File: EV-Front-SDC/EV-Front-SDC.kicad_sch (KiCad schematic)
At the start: 27 parts, among them J1 JST-XA, J2 JST-XA, J3 JST-XA, J4 JST-XA, J5 JST-XA, J6 IMU, J7 GPS, J8 Conn_01x14, Q1 BSS205N, Q2 BSS205N, Q3 BSS205N, U2 MCP23S08-E_SS

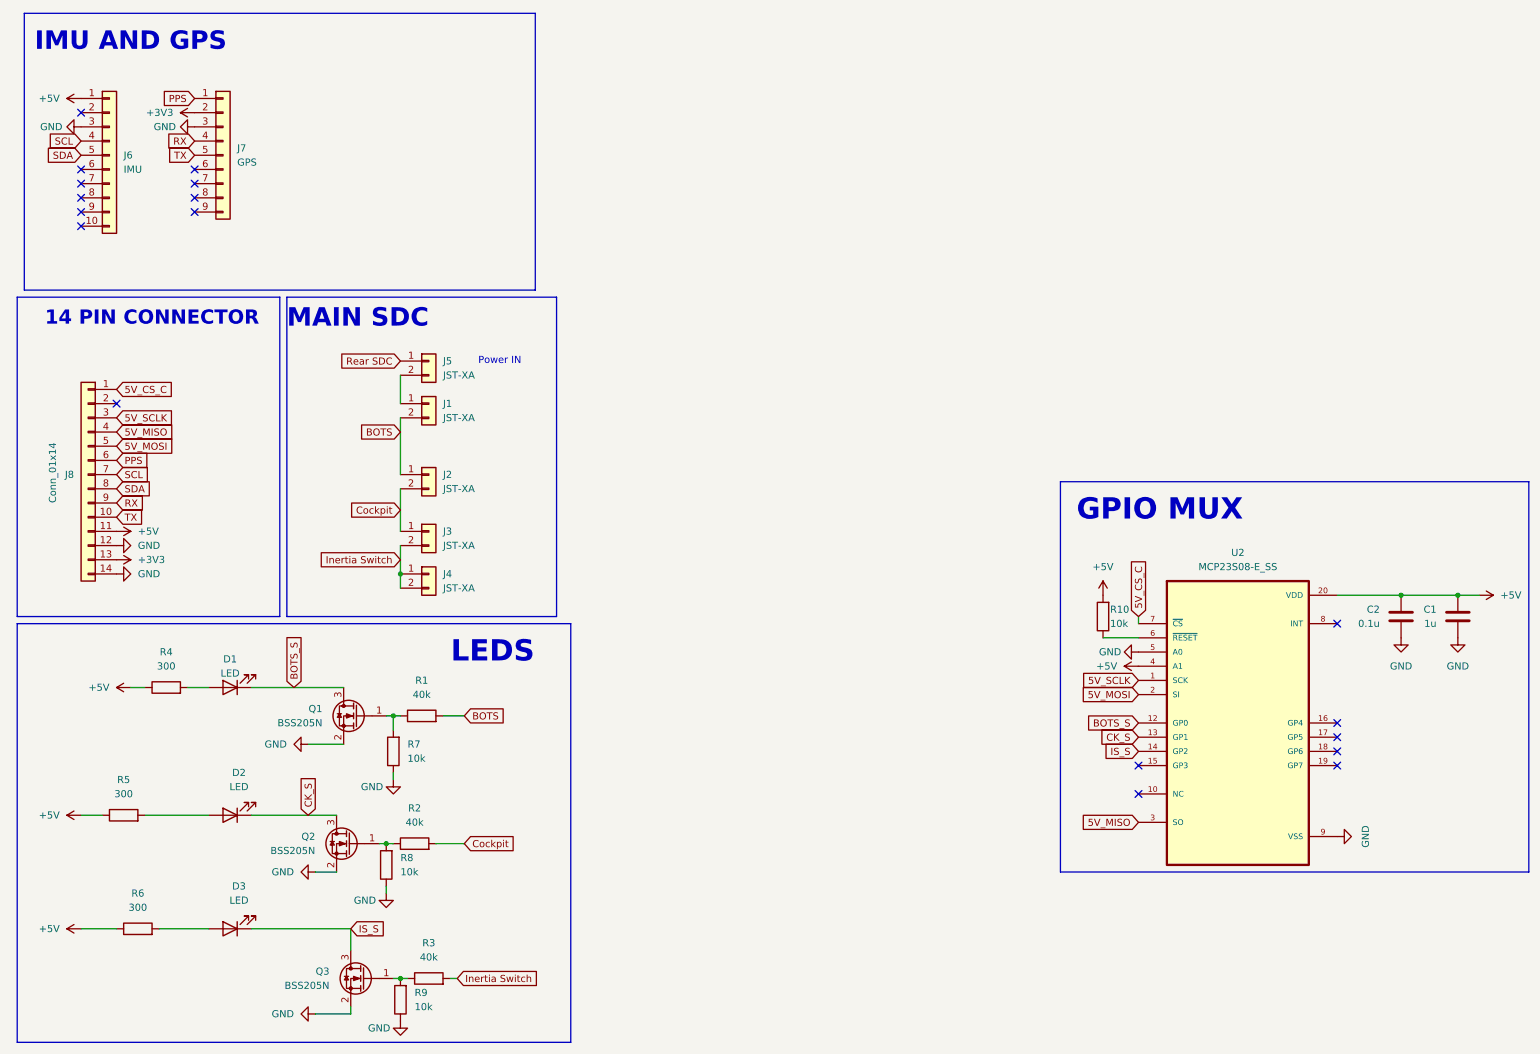
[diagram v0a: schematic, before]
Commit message: - SDC loop now on one connector - Added new IMU
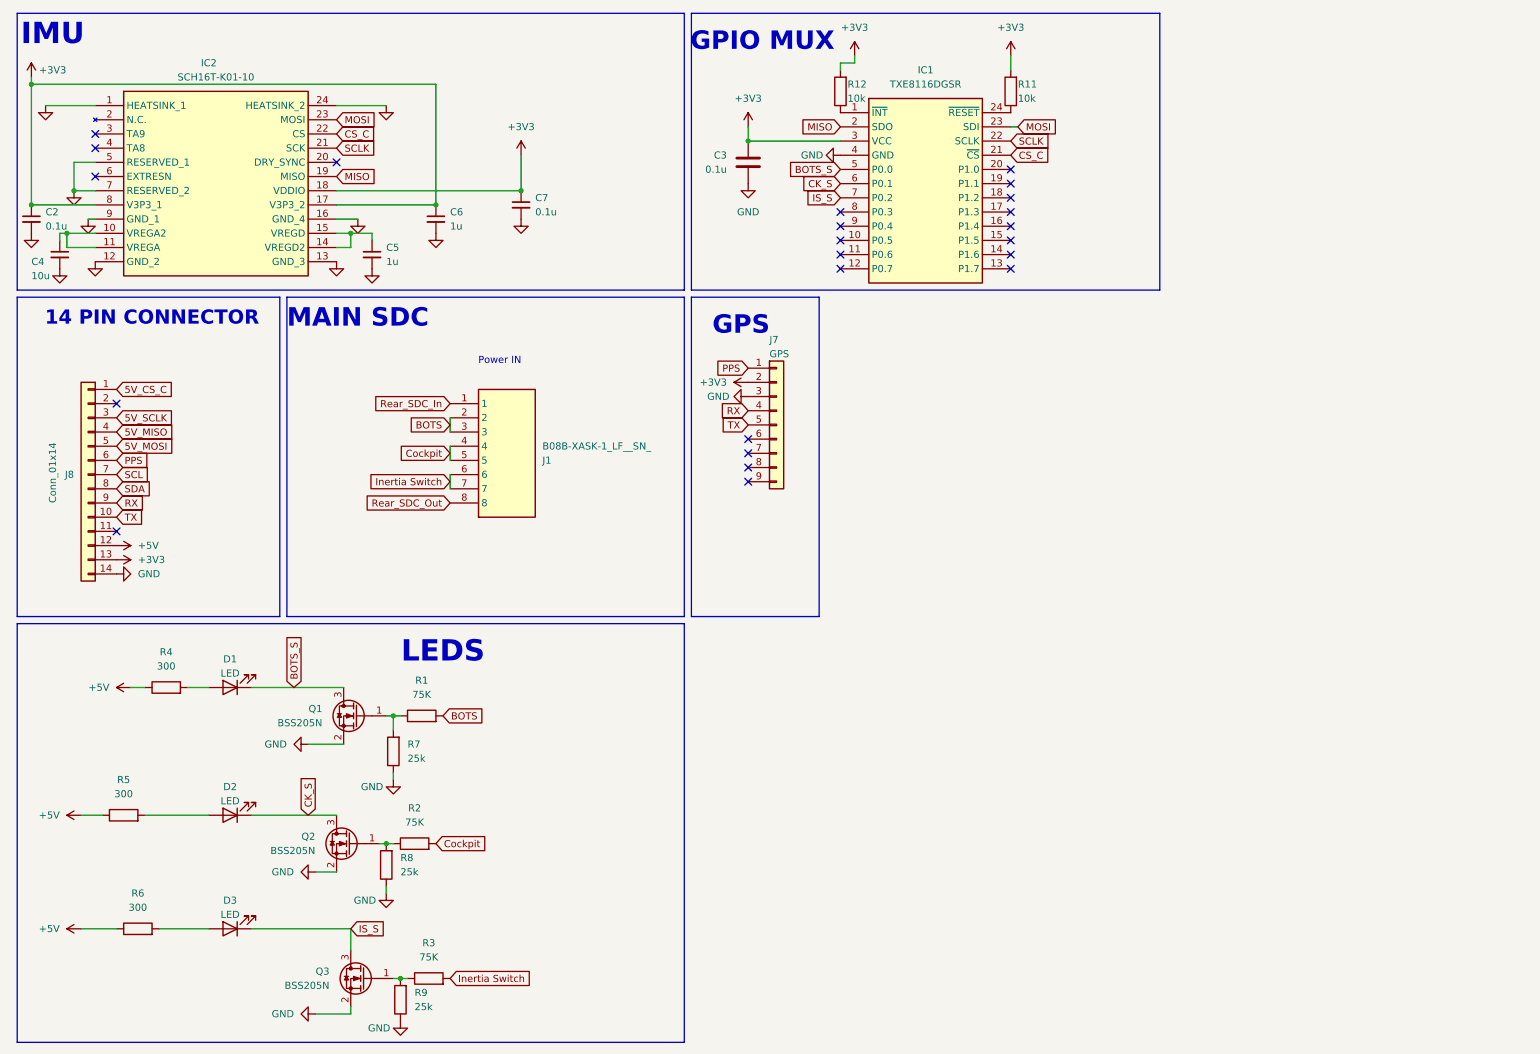
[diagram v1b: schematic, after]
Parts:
- removed C1: 1u, symbol Device:C
- removed C2: 0.1u, symbol Device:C
- removed J1, J2, J3, J4, J5: JST-XA, Custom_MSM:Connector_JST-XA_2POS, symbol Custom_MSM1:Connector_JST-XA_2POS
- removed J6: IMU, CustomFootprints10:IMU, symbol Connector_Generic:Conn_01x10
- removed R10: 10k, symbol Device:R
- removed U2: MCP23S08-E_SS, symbol MCP23S08-E_SS:MCP23S08-E_SS
- added C2, C7: 0.1u, Capacitor_SMD:C_0603_1608Metric, symbol Device:C_Small
- added C3: 0.1u, Capacitor_SMD:C_0603_1608Metric, symbol Device:C
- added C4: 10u, Capacitor_SMD:C_0603_1608Metric, symbol Device:C_Small
- added C5, C6: 1u, Capacitor_SMD:C_0603_1608Metric, symbol Device:C_Small
- added IC1: TXE8116DGSR, SOP50P490X110-24N, symbol Custom_MSM1:TXE8116DGSR
- added IC2: SCH16T-K01-10, Custom_MSM:SCH16TK0110, symbol SCH16T-K01-10:SCH16T-K01-10
- added J1: B08B-XASK-1_LF__SN_, B08BXASK1LFSN, symbol B08B-XASK-1_LF__SN_:B08B-XASK-1_LF__SN_
- added R11, R12: 10k, Resistor_SMD:R_0603_1608Metric, symbol Device:R
- D1, D2, D3: footprint (none) -> LED_SMD:LED_0603_1608Metric; MFN (none) -> LR Q976.01; S1PL (none) -> https://www.mouser.co.uk/en/ProductDetail/ams-OSRAM/LR-Q976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; S1PN (none) -> 720-LRQ976.01; S2PL (none) -> http://digikey.co.uk/en/products/detail/ams-osram-ag/LR-Q97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; S2PN (none) -> 475-LRQ976.01-P2R2-1CT-ND
- J8: MFN (none) -> B14B-XASK-1 (LF)(SN); S1PL (none) -> https://uk.rs-online.com/web/p/pcb-headers/6027837; S1PN (none) -> 602-7837
- R1, R2, R3: value 40k -> 75K; footprint (none) -> Resistor_SMD:R_0603_1608Metric; MFN (none) -> TNPW060375K0BHEA; S1PL (none) -> https://www.mouser.co.uk/en/ProductDetail/Vishay/TNPW060375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; S1PN (none) -> 71-TNPW060375K0BHEA; S2PL (none) -> https://www.digikey.co.uk/en/products/detail/vishay-dale/tn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; S2PN (none) -> 541-TNPW060375K0BHEACT-ND
- R4, R5, R6: footprint (none) -> Resistor_SMD:R_0603_1608Metric; MFN (none) -> CRCW0603300RJNEAHP; S1PL (none) -> https://www.mouser.co.uk/en/ProductDetail/Vishay/CRCW060330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; S1PN (none) -> 71-CRCW0603300RJNEAH; S2PL (none) -> https://www.digikey.co.uk/en/products/detail/vishay-dale/CR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; S2PN (none) -> 541-300SATR-ND
- R7, R8, R9: value 10k -> 25k; footprint (none) -> Resistor_SMD:R_0603_1608Metric; MFN (none) -> PTN0603H2502BST1; S1PL (none) -> https://www.mouser.co.uk/en/ProductDetail/Vishay-Thin-Film/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; S1PN (none) -> Images are for reference only See Product Specifications Mo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
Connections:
- net +3V3: now also C2.1, C3.1, C6.1, C7.1, IC1.3 (VCC), IC2.17 (V3P3_2), IC2.18 (VDDIO), IC2.8 (V3P3_1), R11.2, R12.2
- net +5V: now also J8.12 (Pin_12); no longer J8.11 (Pin_11)
- net BOTS: now also J1.2, J1.3
- net BOTS_S: now also IC1.5 (P0.0)
- net CK_S: now also IC1.6 (P0.1)
- net Cockpit: now also J1.4, J1.5
- net GND: now also C2.2, C3.2, C4.2, C5.2, C6.2, C7.2, IC1.4 (GND), IC2.1 (HEATSINK_1), IC2.12 (GND_2), IC2.13 (GND_3), IC2.16 (GND_4), IC2.24 (HEATSINK_2), IC2.5 (RESERVED_1), IC2.7 (RESERVED_2), IC2.9 (GND_1); no longer J8.12 (Pin_12)
- net IS_S: now also IC1.7 (P0.2)
- net Inertia Switch: now also J1.6, J1.7
- new net: IC1.1 (~{INT}), R12.1
- new net: IC1.24 (~{RESET}), R11.1
- new net: C4.1, IC2.10 (VREGA2), IC2.11 (VREGA)
- new net: C5.1, IC2.14 (VREGD2), IC2.15 (VREGD)
- new net CS_C: IC1.21 (~{CS}), IC2.22 (CS)
- new net MISO: IC1.2 (SDO), IC2.19 (MISO)
- new net MOSI: IC1.23 (SDI), IC2.23 (MOSI)
- new net Rear_SDC_In: J1.1
- new net Rear_SDC_Out: J1.8
- new net SCLK: IC1.22 (SCLK), IC2.21 (SCK)
- no-connect marks 18 -> 23
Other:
- note added: "GPS"
- note added: "IMU"
- note removed: "IMU AND GPS"

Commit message: Add files via upload
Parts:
- added C11, C12: 0.1u, Capacitor_SMD:C_0603_1608Metric, symbol Device:C
- added C13: 1u, Capacitor_SMD:C_0603_1608Metric, symbol Device:C
- added U3: MAX3390EEUD_T, customFootprints:SOP65P640X110-14N, symbol MAX3390EEUD_T:MAX3390EEUD_T
- U1: renamed from IC1; Mouser Part Number (none) -> 595-TXE8116DGSR; Mouser Price/Stock (none) -> https://www.mouser.co.uk/en/ProductDetail/Texas-Instruments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
- renumbered J7 to J2, J8 to J3, IC2 to U2
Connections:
- net +3V3: now also C11.1, U3.1 (VL), U3.8 (~{THREE}-STATE); no longer R11.2, R12.2
- net +5V: now also R11.2, R12.2, C12.1, C13.1, U3.14 (VCC)
- net 5V_MISO: now also U3.13 (I_VCC1)
- net 5V_MOSI: now also U3.12 (O_VCC2)
- net 5V_SCLK: now also U3.11 (O_VCC3)
- net CS_C: no longer U2.22 (CS)
- net GND: now also C11.2, U3.7 (GND)
- net MISO: now also U3.2 (O_VL1)
- net MOSI: now also U3.3 (I_VL2)
- net SCLK: now also U3.4 (I_VL3)
- net 5V_CS_D: now reaches J3.2 (Pin_2)
- net 5V_CS_D: now also U3.10 (O_VCC4)
- net SCL: no longer names the net of J3.7 (Pin_7)
- net SDA: no longer names the net of J3.8 (Pin_8)
- new net: C12.2, C13.2
- new net CS_D: U2.22 (CS), U3.5 (I_VL4)
- no-connect marks 23 -> 22
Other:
- note added: "Level-Shifter"

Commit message: Made SDC Routing changes
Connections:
- net Inertia Switch: no longer J1.6, J1.7
- net Rear_SDC_Out: no longer names the net of J1.8
- new net Inertia Switch (Out): J1.6
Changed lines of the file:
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@@
-	(wire
-		(pts
-			(xy 90.17 95.25) (xy 90.17 97.79)
-		)
-		(stroke
-			(width 0)
-			(type default)
-		)
-	)
 	(wire
 		(pts
@@
 		)
 	)
-	(global_label "Rear_SDC_Out"
-		(shape input)
-		(at 90.17 100.33 180)
-		(effects
-			(font
-				(size 1.27 1.27)
-			)
-			(justify right)
-		)
-		(property "Intersheetrefs" "${INTERSHEET_REFS}"
-			(at 81.8025 109.22 0)
-			(hide yes)
-			(show_name no)
-			(do_not_autoplace no)
-			(effects
-				(font
-					(size 1.27 1.27)
-				)
-				(justify right)
-			)
-		)
-	)
 	(global_label "5V_SCLK"
 		(shape input)
@@
 		)
 	)
-	(global_label "Inertia Switch"
-		(shape input)
-		(at 90.17 96.52 180)
-		(fields_autoplaced yes)
-		(effects
-			(font
-				(size 1.27 1.27)
-			)
-			(justify right)
-		)
-		(property "Intersheetrefs" "${INTERSHEET_REFS}"
-			(at 82.4072 96.52 0)
-			(hide yes)
-			(show_name no)
-			(do_not_autoplace no)
-			(effects
-				(font
-					(size 1.27 1.27)
-				)
-				(justify right)
-			)
-		)
-	)
 	(global_label "5V_CS_D"
 		(shape input)
@@
 			)
 		)
+	)
+	(global_label "Inertia Switch (Out)"
+		(shape input)
+		(at 90.17 95.25 180)
+		(effects
+			(font
+				(size 1.27 1.27)
+			)
+			(justify right)
+		)
+		(property "Intersheetrefs" "${INTERSHEET_REFS}"
+			(at 81.8025 104.14 0)
+			(hide yes)
+			(show_name no)
+			(do_not_autoplace no)
+			(effects
+				(font
+					(size 1.27 1.27)
+				)
+				(justify right)
+			)
+		)

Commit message: Routed the PCB
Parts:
- removed J1: B08B-XASK-1_LF__SN_, B08BXASK1LFSN, symbol B08B-XASK-1_LF__SN_:B08B-XASK-1_LF__SN_
- added J1: B06B-PASK_LF__SN_, Custom_MSM:S06BXASK1LFSN, symbol B06B-PASK_LF__SN_:B06B-PASK_LF__SN_
- C11, C12, C13, C2, C3, C4, C5, C6, C7: footprint Capacitor_SMD:C_0603_1608Metric -> Capacitor_SMD:C_0805_2012Metric
- D1, D2, D3: footprint LED_SMD:LED_0603_1608Metric -> LED_SMD:LED_0805_2012Metric
- R1, R11, R12, R2, R3, R4, R5, R6, R7, R8, R9: footprint Resistor_SMD:R_0603_1608Metric -> Resistor_SMD:R_0805_2012Metric
- U1: footprint SOP50P490X110-24N -> Package_DFN_QFN:QFN-24-1EP_4x4mm_P0.5mm_EP2.7x2.7mm
- U3: footprint customFootprints:SOP65P640X110-14N -> Custom_MSM:SOP65P640X110-14N
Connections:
- net CS_C is gone; now on net 5V_CS_C: U1.21 (~{CS})
- net +3V3: no longer C3.1, U1.3 (VCC)
- net +5V: now also C3.1, U1.3 (VCC)
- net 5V_MISO: now also U1.2 (SDO)
- net 5V_MOSI: now also U1.23 (SDI)
- net 5V_SCLK: now also U1.22 (SCLK)
- net BOTS: now also J1.2, J1.3
- net Cockpit: now also J1.4, J1.5
- net Inertia Switch: now also J1.6
- net MISO: no longer U1.2 (SDO)
- net MOSI: no longer U1.23 (SDI)
- net SCLK: no longer U1.22 (SCLK)
- new net Rear_SDC_In(Right): J1.1
- no-connect marks 22 -> 24

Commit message: Fixed GPIO footprint + added signature
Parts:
- removed U1: TXE8116DGSR, Package_DFN_QFN:QFN-24-1EP_4x4mm_P0.5mm_EP2.7x2.7mm, symbol Custom_MSM1:TXE8116DGSR
- added U1: (no value), Package_DFN_QFN:QFN-24-1EP_4x4mm_P0.5mm_EP2.7x2.7mm, symbol Custom_MSM1:TXE8116RGER
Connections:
- net +5V: now also U1.18 (VCC)
- net 5V_CS_C: now also U1.12 (CS)
- net 5V_MISO: now also U1.17 (SDO)
- net 5V_MOSI: now also U1.14 (SDI)
- net 5V_SCLK: now also U1.13 (SCLK)
- net BOTS_S: now also U1.20 (P0.0)
- net CK_S: now also U1.21 (P0.1)
- net GND: now also C12.2, C13.2, U1.19 (GND)
- net IS_S: now also U1.22 (P0.2)
- net at R12.1: now also U1.16 (INT)
- net at R11.1: now also U1.15 (RESET)

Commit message: Re-routed and bomed
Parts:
- removed C11, C12, C3: 0.1u, Capacitor_SMD:C_0805_2012Metric, symbol Device:C
- removed C13: 1u, Capacitor_SMD:C_0805_2012Metric, symbol Device:C
- removed C2: 0.1u, Capacitor_SMD:C_0805_2012Metric, symbol Device:C_Small
- removed J1: B06B-PASK_LF__SN_, Custom_MSM:S06BXASK1LFSN, symbol B06B-PASK_LF__SN_:B06B-PASK_LF__SN_
- removed U1: (no value), Package_DFN_QFN:QFN-24-1EP_4x4mm_P0.5mm_EP2.7x2.7mm, symbol Custom_MSM1:TXE8116RGER
- added C1, C7, C8: 0.1u, Capacitor_SMD:C_0805_2012Metric, symbol Device:C_Small
- added C4, C9: 1u, Capacitor_SMD:C_0805_2012Metric, symbol Device:C_Small
- added J2: Conn_01x06, Connector_JST:JST_XA_S06B-XASK-1_1x06_P2.50mm_Horizontal, symbol Connector_Generic:Conn_01x06
- added U2: (no value), Package_DFN_QFN:QFN-24-1EP_4x4mm_P0.5mm_EP2.7x2.7mm, symbol Custom_MSM1:TXE8116RGER
- C2: renamed from C4; MFP (none) -> VJ0805Y106KXQTW1BC; S1PL (none) -> https://www.mouser.co.uk/en/ProductDetail/Vishay-Vitramon/V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; S1PN (none) -> 77-VJ0805Y106KXQTWBC; S1PRICE (none) -> 0.361; S2PL (none) -> https://www.digikey.co.uk/en/products/detail/vishay-vitramo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; S2PN (none) -> 720-VJ0805Y106KXQTW1BCTR-ND; S2PRICE (none) -> 0.38
- C3: renamed from C5; MFP (none) -> VJ0805Y105KXQTW1BC; S1PL (none) -> https://www.mouser.co.uk/en/ProductDetail/Vishay-Vitramon/V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; S1PN (none) -> 77-VJ0805Y105KXQTBC; S1PRICE (none) -> 0.196; S2PL (none) -> https://www.digikey.co.uk/en/products/detail/vishay-vitramo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; S2PN (none) -> 720-1757-1-ND; S2PRICE (none) -> 0.160
- C5: renamed from C7; MFP (none) -> GA0805Y104JXABT31G; S1PL (none) -> https://www.mouser.co.uk/en/ProductDetail/Vishay-Vitramon/G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; S1PN (none) -> 77-GA805Y104JXABT31G; S1PRICE (none) -> 0.37; S2PL (none) -> https://www.digikey.co.uk/en/products/detail/vishay-vitramo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; S2PN (none) -> 720-GA0805Y104JXABT31GCT-ND; S2PRICE (none) -> 0.368
- C6: value 1u -> 0.1u; MFP (none) -> GA0805Y104JXABT31G; S1PL (none) -> https://www.mouser.co.uk/en/ProductDetail/Vishay-Vitramon/G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; S1PN (none) -> 77-GA805Y104JXABT31G; S1PRICE (none) -> 0.37; S2PL (none) -> https://www.digikey.co.uk/en/products/detail/vishay-vitramo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; S2PN (none) -> 720-GA0805Y104JXABT31GCT-ND; S2PRICE (none) -> 0.368
- J3: renamed from J2; MFP (none) -> 746; S1PL (none) -> https://www.mouser.co.uk/en/ProductDetail/Adafruit/746?qs=G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; S1PN (none) -> 485-746; S1PRICE (none) -> 22.49; S2PL (none) -> https://www.digikey.co.uk/en/products/detail/adafruit-indus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; S2PN (none) -> 1528-1153-ND; S2PRICE (none) -> 22.38
- R1, R2, R3: value 75K -> 300R; MFN TNPW060375K0BHEA -> CRCW0805300RFKEA; S1PL https://www.mouser.co.uk/en/ProductDetail/Vishay/TNPW060375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 -> https://www.mouser.co.uk/en/ProductDetail/Vishay/CRCW080530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; S1PN 71-TNPW060375K0BHEA -> 71-CRCW0805300RFKEA; S1PRICE (none) -> 0.075; S2PL https://www.digikey.co.uk/en/products/detail/vishay-dale/tn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 -> https://www.digikey.co.uk/en/products/detail/vishay-dale/CR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; S2PN 541-TNPW060375K0BHEACT-ND -> 541-300CTR-ND; S2PRICE (none) -> 0.07
- R4, R5, R6: value 300 -> 25k; MFN CRCW0603300RJNEAHP -> PNM0805E2502BST1; S1PL https://www.mouser.co.uk/en/ProductDetail/Vishay/CRCW060330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 -> https://www.mouser.co.uk/en/ProductDetail/Vishay-Thin-Film/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; S1PN 71-CRCW0603300RJNEAH -> 71-PNM0805E2502BST1; S1PRICE (none) -> 0.834; S2PL https://www.digikey.co.uk/en/products/detail/vishay-dale/CR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 -> https://www.digikey.co.uk/en/products/detail/vishay-dale-th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; S2PN 541-300SATR-ND -> 764-PNM0805E2502BST1TR-ND; S2PRICE (none) -> 0.78
- R7, R8, R9: value 25k -> 75K; MFN PTN0603H2502BST1 -> CRCW080575K0JNEA; S1PL https://www.mouser.co.uk/en/ProductDetail/Vishay-Thin-Film/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 -> https://www.mouser.co.uk/en/ProductDetail/Vishay/TNPW060375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; S1PN Images are for reference only See Product Specifications Mo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 -> 71-CRCW080575K0JNEA; S1PRICE (none) -> 0.075; S2PL (none) -> https://www.digikey.co.uk/en/products/detail/vishay-dale/CR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; S2PN (none) -> 541-75KACT-ND; S2PRICE (none) -> 0.07
- renumbered J3 to J1, Q2 to Q1, Q1 to Q2, R12 to R10, U2 to U1
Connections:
- net +3V3: now also C1.1, C4.1, C7.1; no longer C6.1
- net +5V: now also C6.1, R1.1, R11.1, R2.1, R3.1, C8.1, C9.1, U2.18 (VCC); no longer R11.2, R4.1, R5.1, R6.1
- net 5V_CS_C: now also U2.12 (CS)
- net 5V_MISO: now also U2.17 (SDO)
- net 5V_MOSI: now also U2.14 (SDI)
- net 5V_SCLK: now also U2.13 (SCLK)
- net BOTS: now also R8.2, J2.2 (Pin_2), J2.3 (Pin_3); no longer R1.2
- net BOTS_S: now also U2.20 (P0.0)
- net CK_S: now also U2.21 (P0.1)
- net Cockpit: now also R7.2, J2.4 (Pin_4), J2.5 (Pin_5); no longer R2.2
- net GND: now also R4.1, R5.1, R6.1, C1.2, C4.2, C7.2, C8.2, C9.2, U2.19 (GND); no longer R7.1, R8.1, R9.1
- net IS_S: now also U2.22 (P0.2)
- net Inertia Switch: now also R9.2, J2.6 (Pin_6); no longer R3.2
- net Rear_SDC_In(Right): now also J2.1 (Pin_1)
- net at D2.2 (A): now also R1.2; no longer R5.2
- net at D1.2 (A): now also R3.2; no longer R4.2
- net at R10.1: now also U2.16 (INT)
- net at D3.2 (A): now also R2.2; no longer R6.2
- new net: Q2.1 (G), R5.2, R8.1
- new net: Q3.1 (G), R6.2, R9.1
- new net: Q1.1 (G), R4.2, R7.1
- new net: R11.2, U2.15 (RESET)
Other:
- moved on the sheet: C5, R10, R11
